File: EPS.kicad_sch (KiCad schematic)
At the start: 30 parts, among them SW101 Deploy_1, SW102 Deploy_2

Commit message: updated battery pack module; updated solar inputs module
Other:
- sheet Battery_Input_1 ports: added BATT_ALERT; removed none
- sheet Battery_Input_2 ports: added BATT_ALERT; removed none
- sheet Interface ports: added {Enables}; removed none
- sheet MCU ports: added MPPT_~{EN}, SOL_STAT_1, SOL_STAT_2; removed none
- sheet Solar_input_1 ports: added STAT_1, STAT_2, ~{EN}; removed none
- sheet Solar_input_2 ports: added STAT_1, STAT_2, ~{EN}; removed none
- sheet Solar_input_3 ports: added STAT_1, STAT_2, ~{EN}; removed none
- sheet Solar_input_4 ports: added STAT_1, STAT_2, ~{EN}; removed none
- sheet Solar_input_5 ports: added STAT_1, STAT_2, ~{EN}; removed none
- sheet Solar_input_6 ports: added STAT_1, STAT_2, ~{EN}; removed none
- note added: "HEADER CHAN"
- note added: "HEADER PV"
- note added: "PC104"
- note removed: "DCDC MODE"
- note removed: "HEAT EN"

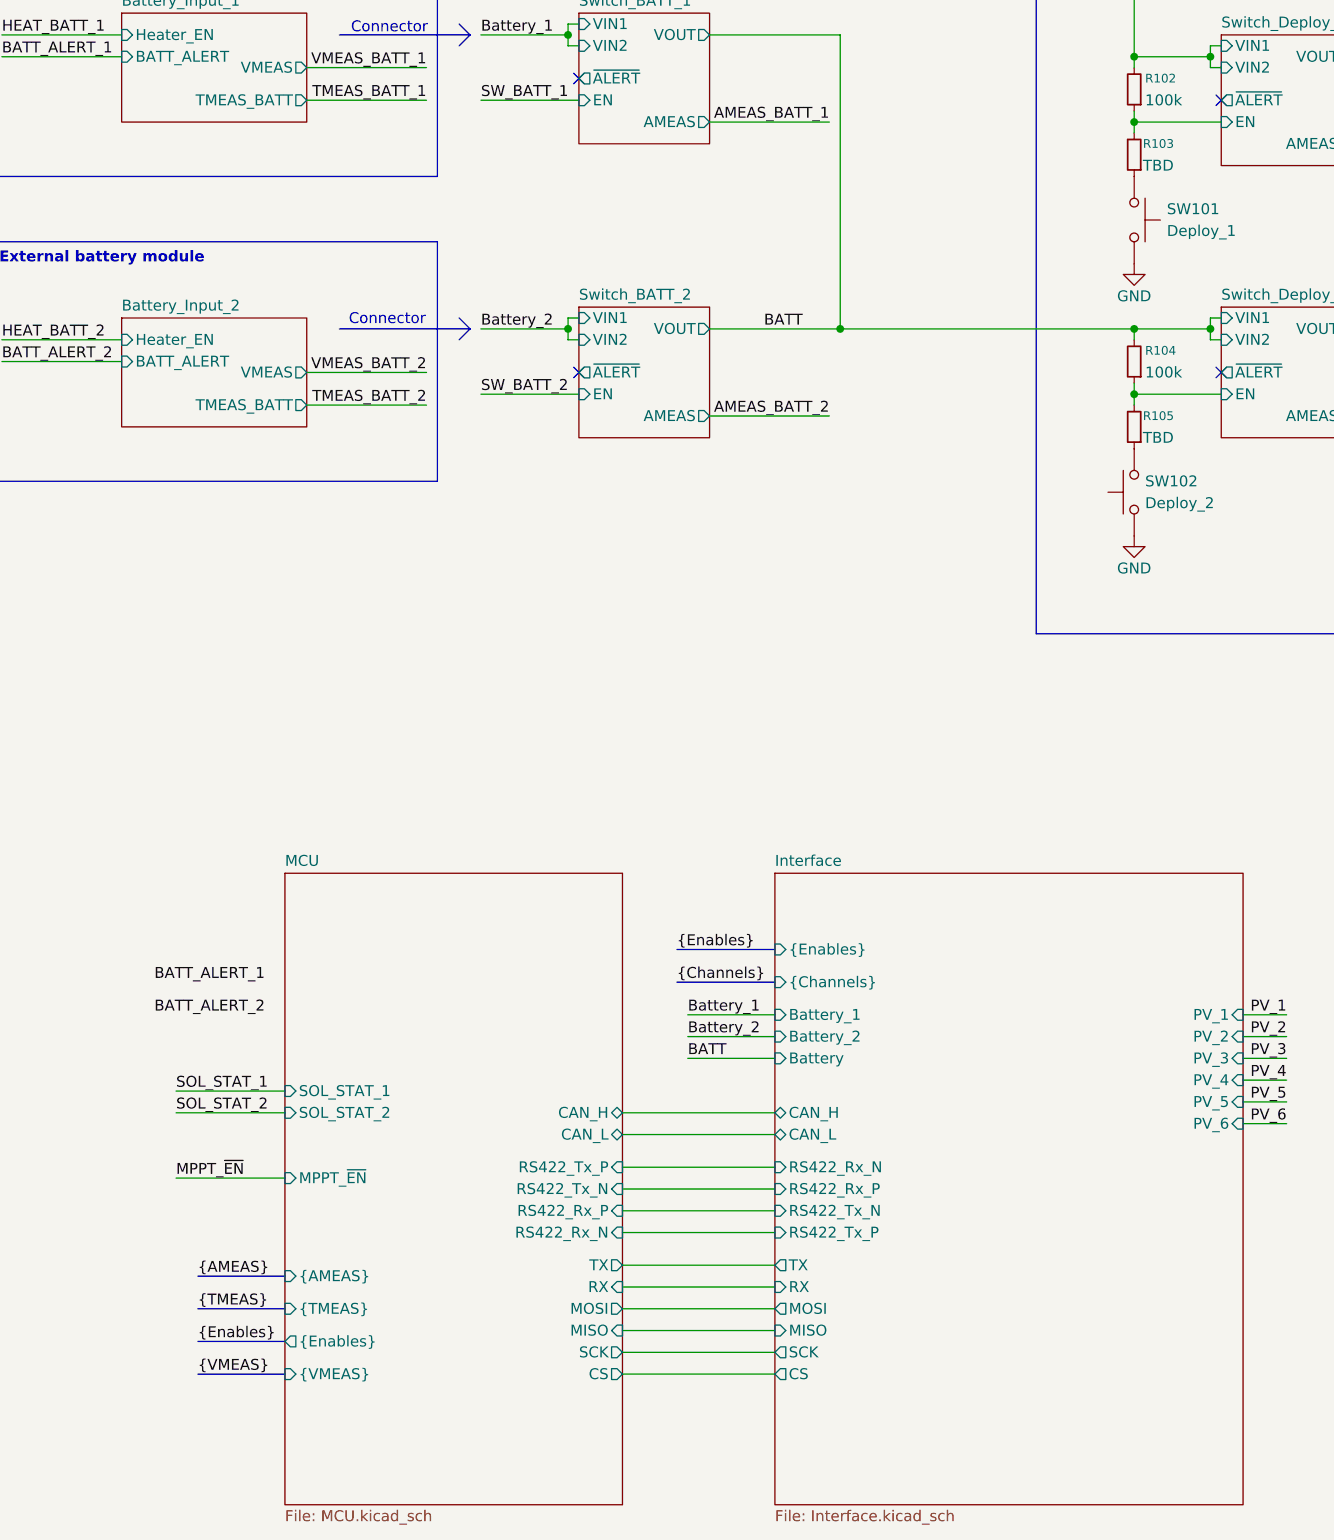
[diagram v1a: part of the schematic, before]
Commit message: added values to most parts
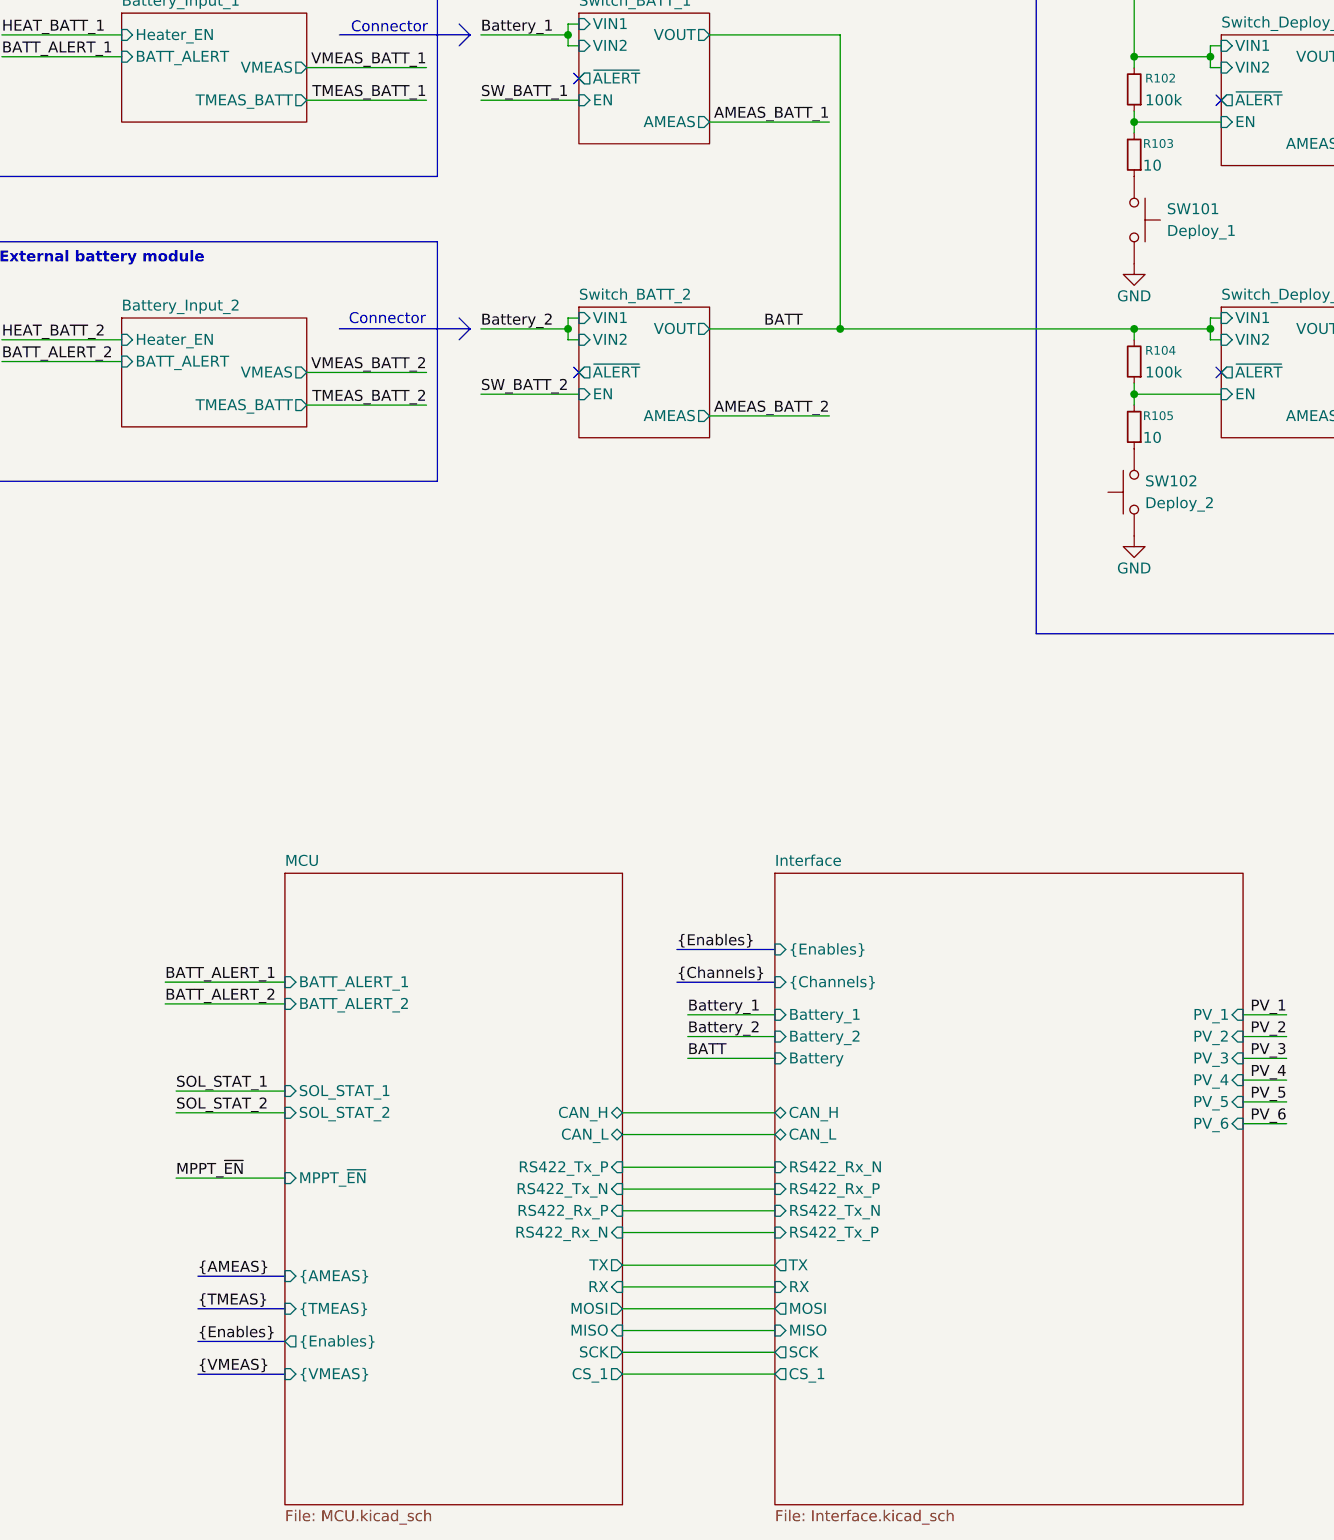
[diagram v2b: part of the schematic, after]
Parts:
- R103, R105: value TBD -> 10
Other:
- sheet Interface ports: added CS_1; removed CS
- sheet MCU ports: added BATT_ALERT_1, BATT_ALERT_2, CS_1; removed CS
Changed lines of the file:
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@@
 	(wire
 		(pts
+			(xy 134.62 161.29) (xy 148.59 161.29)
+		)
+		(stroke
+			(width 0)
+			(type default)
+		)
+	)
+	(wire
+		(pts
 			(xy 40.64 144.78) (xy 53.34 144.78)
 		)
@@
 		)
 	)
+	(wire
+		(pts
+			(xy 134.62 158.75) (xy 148.59 158.75)
+		)
+		(stroke
+			(width 0)
+			(type default)
+		)
+	)
 	(polyline
 		(pts
@@
 	)
 	(label "BATT_ALERT_1"
-		(at 133.35 158.75 0)
+		(at 134.62 158.75 0)
 		(effects
 			(font
@@
 	)
 	(label "BATT_ALERT_2"
-		(at 133.35 162.56 0)
+		(at 134.62 161.29 0)
 		(effects
 			(font
@@
 			)
 		)
-		(property "Value" "TBD"
+		(property "Value" "10"
 			(at 248.666 63.5 0)
 			(effects
@@
 			)
 		)
-		(property "Value" "TBD"
+		(property "Value" "10"
 			(at 248.666 95.25 0)
 			(effects
@@
 			)
 		)
-		(pin "CS" output
+		(pin "CS_1" output
 			(at 187.96 204.47 0)
 			(effects
@@
 			)
 		)
+		(pin "BATT_ALERT_1" input
+			(at 148.59 158.75 180)
+			(effects
+				(font
+					(size 1.27 1.27)
+				)
+				(justify left)
+			)
+		)
+		(pin "BATT_ALERT_2" input
+			(at 148.59 161.29 180)
+			(effects
+				(font
+					(size 1.27 1.27)
+				)
+				(justify left)
+			)
+		)
 		(instances
 			(project "EPS"
@@
 			)
 		)
-		(pin "CS" output
+		(pin "CS_1" output
 			(at 205.74 204.47 180)
 			(effects

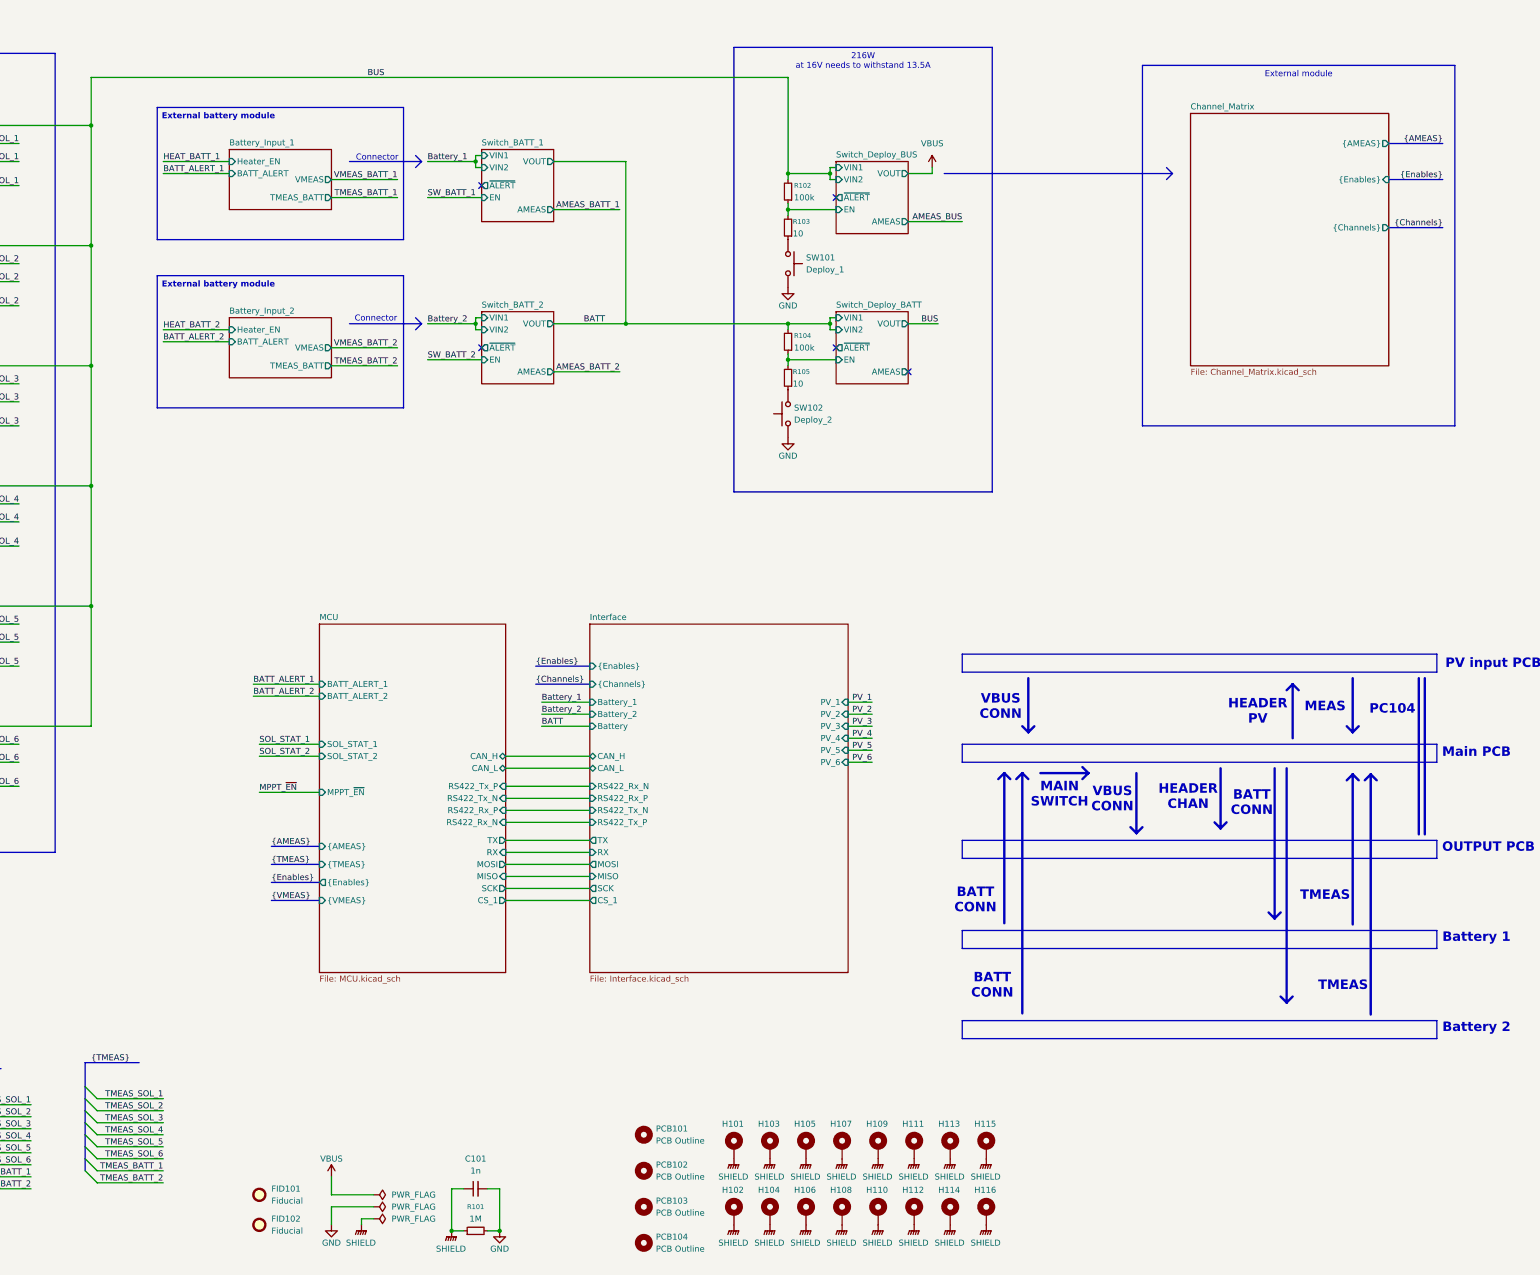
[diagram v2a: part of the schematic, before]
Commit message: deleted unused sheets, added standalone current measure sheet
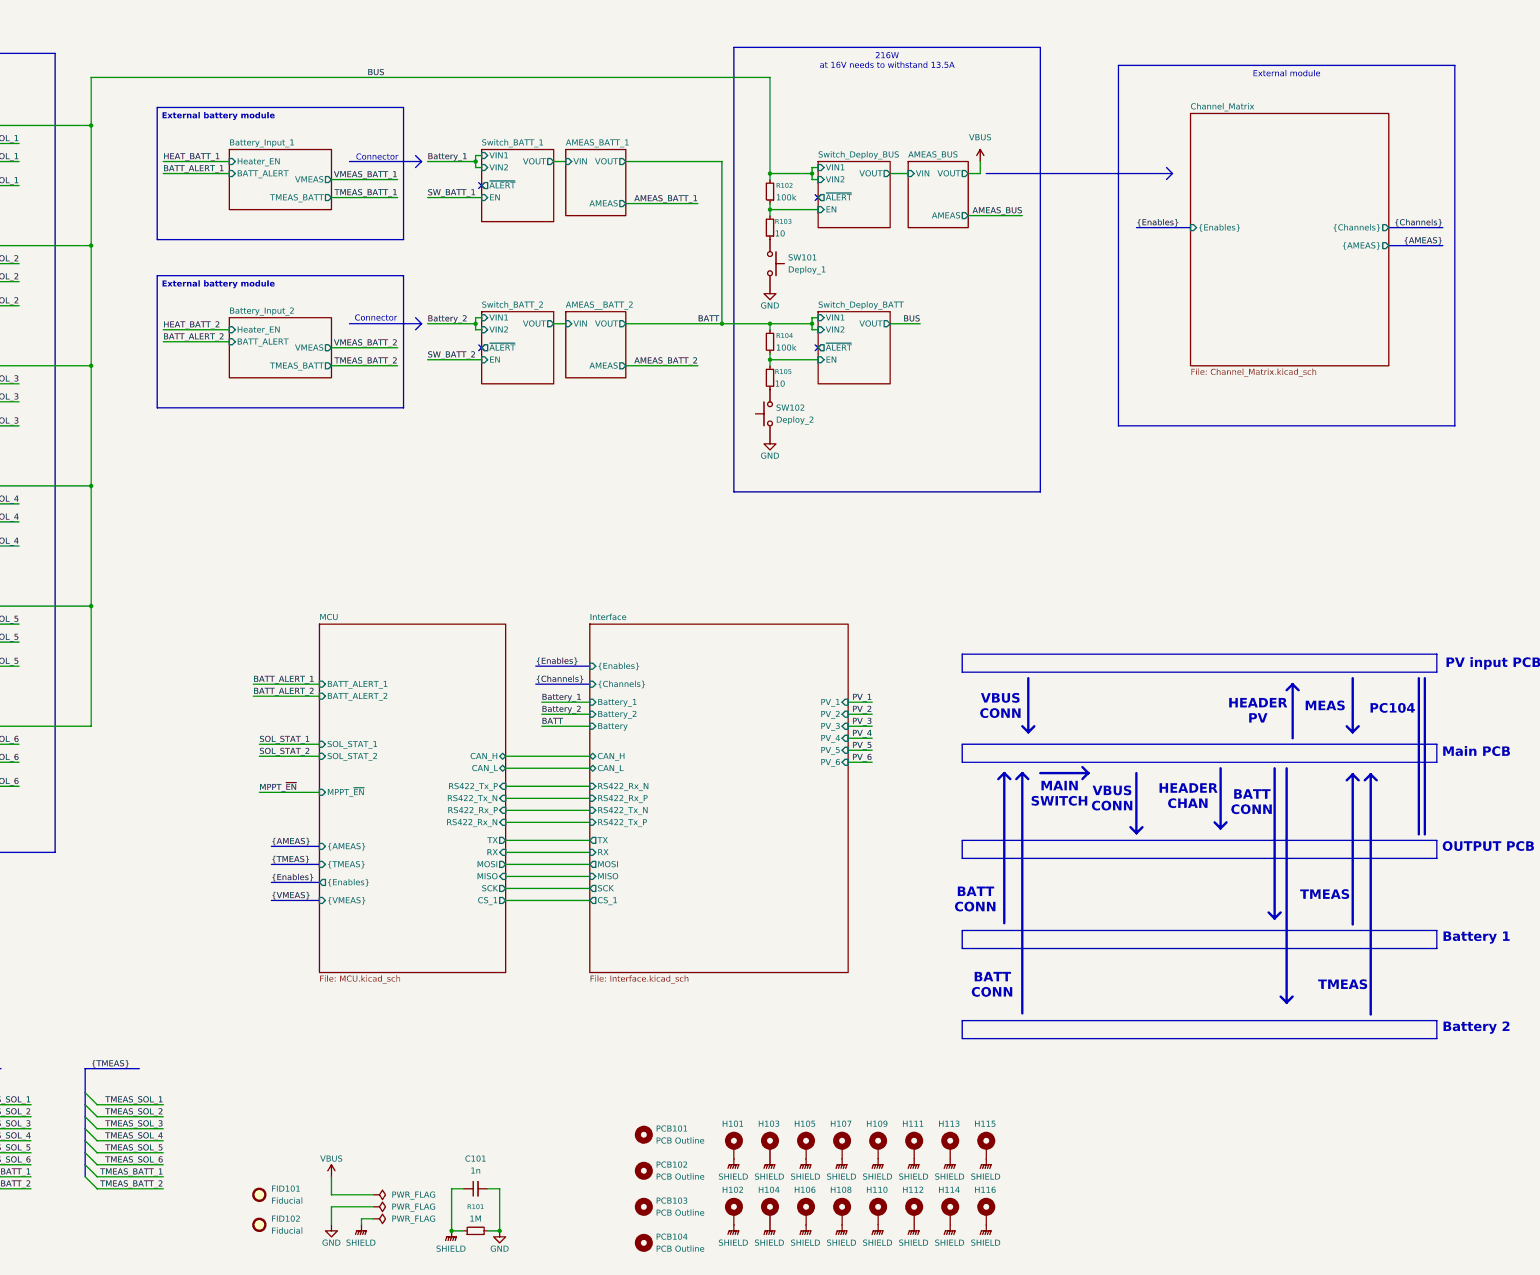
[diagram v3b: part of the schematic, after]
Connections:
- no-connect marks 5 -> 4
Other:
- added sheet AMEAS_BATT_1 (Current_Measure.kicad_sch)
- added sheet AMEAS_BUS (Current_Measure.kicad_sch)
- added sheet AMEAS__BATT_2 (Current_Measure.kicad_sch)
- sheet Switch_BATT_1 ports: added none; removed AMEAS
- sheet Switch_BATT_2 ports: added none; removed AMEAS
- sheet Switch_Deploy_BATT ports: added none; removed AMEAS
- sheet Switch_Deploy_BUS ports: added none; removed AMEAS
- moved on the sheet: R102, R103, R104, R105, SW101, SW102

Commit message: minor adjustments
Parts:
- added FID103, FID104, FID105, FID106, FID107, FID108: Fiducial, Fiducial:Fiducial_1mm_Mask2mm, symbol Mechanical:Fiducial
- FID101, FID102: footprint (none) -> Fiducial:Fiducial_1mm_Mask2mm
- SW101: value Deploy_1 -> Deploy
- SW102: value Deploy_2 -> Deploy
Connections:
- net GND: now also SW102.2; no longer SW102.1
- net at R105.1: now also SW102.1; no longer SW102.2
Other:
- moved on the sheet: C101, FID101, FID102, R101
